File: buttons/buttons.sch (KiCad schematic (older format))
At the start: 9 parts, among them J1 header

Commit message: more library changes
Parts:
- J1: footprint HDRV9W63P0X254_1X9_2286X369X950P -> buttons:header
- S1, S2: footprint OS103011MS8QP1 -> buttons:switch
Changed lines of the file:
@@
 F 0 "S1" H 6928 2096 50  0000 L CNN
 F 1 "switch" H 6928 2005 50  0000 L CNN
-F 2 "OS103011MS8QP1" H 6950 2400 50  0001 L CNN
+F 2 "buttons:switch" H 6950 2400 50  0001 L CNN
 F 3 "https://www.ckswitches.com/media/1428/os.pdf" H 6950 2300 50  0001 L CNN
 F 4 "C & K COMPONENTS - OS103011MS8QP1 - SWITCH, SP3T, 0.1A, 12VDC, PCB, ON-ON-ON" H 6950 2200 50  0001 L CNN "Description"
@@
 F 0 "S2" H 6928 2946 50  0000 L CNN
 F 1 "switch" H 6928 2855 50  0000 L CNN
-F 2 "OS103011MS8QP1" H 6950 3250 50  0001 L CNN
+F 2 "buttons:switch" H 6950 3250 50  0001 L CNN
 F 3 "https://www.ckswitches.com/media/1428/os.pdf" H 6950 3150 50  0001 L CNN
 F 4 "C & K COMPONENTS - OS103011MS8QP1 - SWITCH, SP3T, 0.1A, 12VDC, PCB, ON-ON-ON" H 6950 3050 50  0001 L CNN "Description"
@@
 F 0 "J1" H 4842 2235 50  0000 C CNN
 F 1 "header" H 4842 2326 50  0000 C CNN
-F 2 "HDRV9W63P0X254_1X9_2286X369X950P" H 5200 3400 50  0001 L CNN
+F 2 "buttons:header" H 5200 3400 50  0001 L CNN
 F 3 "https://componentsearchengine.com/Datasheets/1/825433-9.pdf" H 5200 3300 50  0001 L CNN
 F 4 "MOD 2 PINHDR 1X9 P." H 5200 3200 50  0001 L CNN "Description"

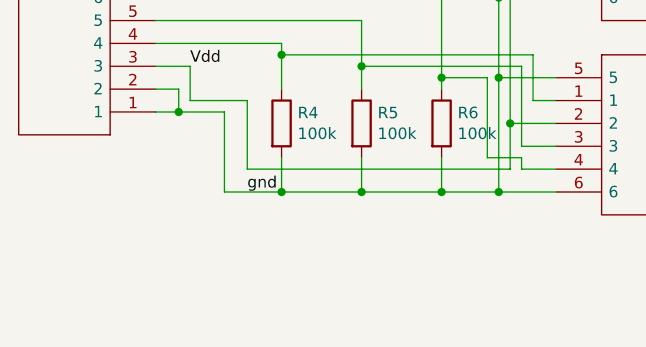
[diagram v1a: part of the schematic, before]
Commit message: cleaned up directories, silkscreen
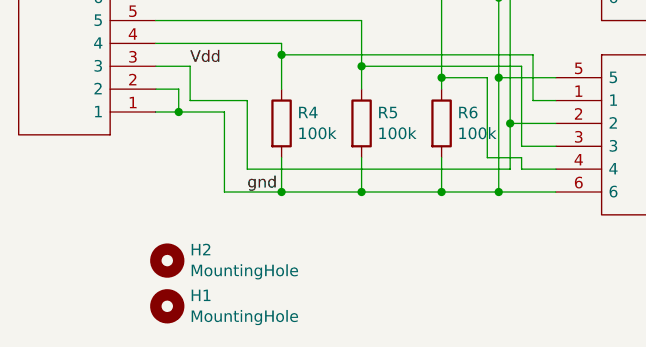
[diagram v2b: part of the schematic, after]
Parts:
- added H1, H2: MountingHole, buttons:MountingHole_2.5mm_Pad, symbol Mechanical:MountingHole
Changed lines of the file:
@@
+	1    0    0    -1
+$EndComp
+$Comp
+L Mechanical:MountingHole H2
+U 1 1 61672EB2
+P 4600 3950
+F 0 "H2" H 4700 3996 50  0000 L CNN
+F 1 "MountingHole" H 4700 3905 50  0000 L CNN
+F 2 "buttons:MountingHole_2.5mm_Pad" H 4600 3950 50  0001 C CNN
+F 3 "~" H 4600 3950 50  0001 C CNN
+	1    4600 3950
+	1    0    0    -1
+$EndComp
+$Comp
+L Mechanical:MountingHole H1
+U 1 1 616738A9
+P 4600 4150
+F 0 "H1" H 4700 4196 50  0000 L CNN
+F 1 "MountingHole" H 4700 4105 50  0000 L CNN
+F 2 "buttons:MountingHole_2.5mm_Pad" H 4600 4150 50  0001 C CNN
+F 3 "~" H 4600 4150 50  0001 C CNN
+	1    4600 4150
 	1    0    0    -1
 $EndComp

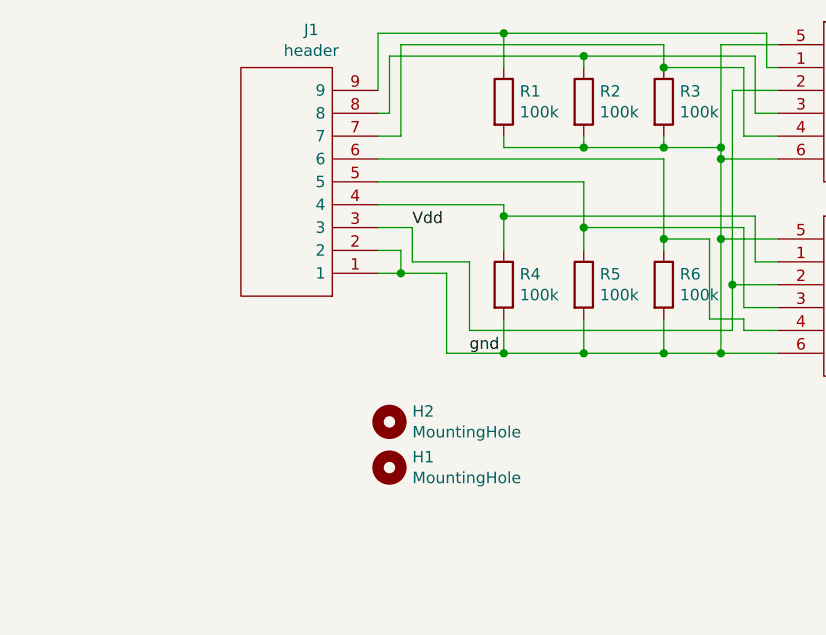
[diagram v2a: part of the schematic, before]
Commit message: Added reset button, fixed 7seg pin order
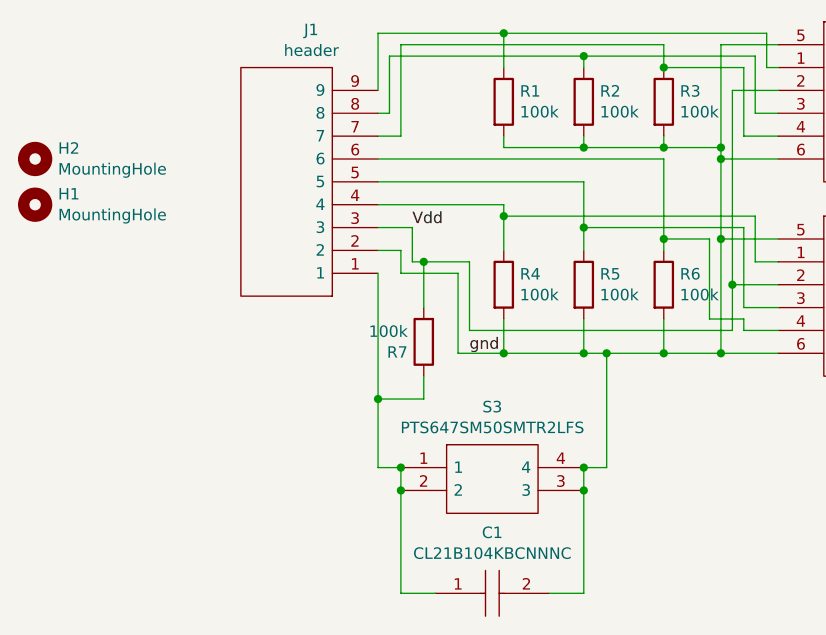
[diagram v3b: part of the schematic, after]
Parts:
- added C1: CL21B104KBCNNNC, CAPC2012X95N, symbol SamacSys_Parts:CL21B104KBCNNNC
- added R7: 100k, SamacSys_Parts:RESC3116X70N, symbol Device:R
- added S3: PTS647SM50SMTR2LFS, PTS647SM50SMTR2LFS, symbol SamacSys_Parts:PTS647SM50SMTR2LFS
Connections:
- net Vdd: now also R7.2
- net gnd: now also C1.2, S3.3, S3.4; no longer J1.1
- new net: C1.1, J1.1, R7.1, S3.1, S3.2
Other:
- moved on the sheet: H1, H2
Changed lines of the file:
@@
 $EndComp
-Wire Wire Line
-	4550 3300 4650 3300
 Wire Wire Line
 	6050 3650 6050 3150
@@
 Wire Wire Line
 	4700 3100 4700 3250
-Wire Wire Line
-	4650 3300 4850 3300
-Wire Wire Line
-	4850 3300 4850 3650
-Wire Wire Line
-	4850 3650 5100 3650
-Connection ~ 4650 3300
 Connection ~ 6050 3650
 Wire Wire Line
-	4700 3250 4950 3250
+	4700 3250 4750 3250
 Wire Wire Line
 	4950 3250 4950 3550
@@
 Connection ~ 5450 3650
 Wire Wire Line
-	5450 3650 5800 3650
+	5450 3650 5550 3650
 Wire Wire Line
 	5800 3500 5800 3650
@@
 Wire Wire Line
 	5100 3500 5100 3650
-Connection ~ 5100 3650
 Wire Wire Line
 	5100 3650 5450 3650
@@
 L Mechanical:MountingHole H2
 U 1 1 61672EB2
-P 4600 3950
-F 0 "H2" H 4700 3996 50  0000 L CNN
-F 1 "MountingHole" H 4700 3905 50  0000 L CNN
-F 2 "buttons:MountingHole_2.5mm_Pad" H 4600 3950 50  0001 C CNN
-F 3 "~" H 4600 3950 50  0001 C CNN
-	1    4600 3950
+P 3050 2800
+F 0 "H2" H 3150 2846 50  0000 L CNN
+F 1 "MountingHole" H 3150 2755 50  0000 L CNN
+F 2 "buttons:MountingHole_2.5mm_Pad" H 3050 2800 50  0001 C CNN
+F 3 "~" H 3050 2800 50  0001 C CNN
+	1    3050 2800
 	1    0    0    -1
 $EndComp
@@
 L Mechanical:MountingHole H1
 U 1 1 616738A9
-P 4600 4150
-F 0 "H1" H 4700 4196 50  0000 L CNN
-F 1 "MountingHole" H 4700 4105 50  0000 L CNN
-F 2 "buttons:MountingHole_2.5mm_Pad" H 4600 4150 50  0001 C CNN
-F 3 "~" H 4600 4150 50  0001 C CNN
-	1    4600 4150
-	1    0    0    -1
-$EndComp
+P 3050 3000
+F 0 "H1" H 3150 3046 50  0000 L CNN
+F 1 "MountingHole" H 3150 2955 50  0000 L CNN
+F 2 "buttons:MountingHole_2.5mm_Pad" H 3050 3000 50  0001 C CNN
+F 3 "~" H 3050 3000 50  0001 C CNN
+	1    3050 3000
+	1    0    0    -1
+$EndComp
+Wire Wire Line
+	4550 4150 4650 4150
+Wire Wire Line
+	4650 4250 4650 4150
+$Comp
+L Device:R R7
+U 1 1 616971F3
+P 4750 3600
+F 0 "R7" H 4820 3646 50  0000 L CNN
+F 1 "100k" H 4820 3555 50  0000 L CNN
+F 2 "SamacSys_Parts:RESC3116X70N" V 4680 3600 50  0001 C CNN
+F 3 "~" H 4750 3600 50  0001 C CNN
+	1    4750 3600
+	-1   0    0    1
+$EndComp
+Wire Wire Line
+	4550 3300 4550 3850
+Wire Wire Line
+	4900 3650 5100 3650
+Connection ~ 5100 3650
+Wire Wire Line
+	4900 3650 4900 3300
+Wire Wire Line
+	4650 3300 4900 3300
+Wire Wire Line
+	4750 3450 4750 3250
+Connection ~ 4750 3250
+Wire Wire Line
+	4750 3250 4950 3250
+Wire Wire Line
+	4750 3750 4750 3850
+Wire Wire Line
+	4750 3850 4550 3850
+Connection ~ 4550 3850
+Wire Wire Line
+	4550 3850 4550 4150
+Wire Wire Line
+	5550 3650 5550 4150
+Wire Wire Line
+	5550 4150 5450 4150
+Connection ~ 5550 3650
+Wire Wire Line
+	5550 3650 5800 3650
+Wire Wire Line
+	5450 4250 5450 4150
+$Comp
+L SamacSys_Parts:CL21B104KBCNNNC C1
+U 1 1 616A684B
+P 4800 4700
+F 0 "C1" H 5050 4965 50  0000 C CNN
+F 1 "CL21B104KBCNNNC" H 5050 4874 50  0000 C CNN
+F 2 "CAPC2012X95N" H 5150 4750 50  0001 L CNN
+F 3 "http://www.samsungsem.com/kr/support/product-search/mlcc/CL21B104KBCNNNC.jsp" H 5150 4650 50  0001 L CNN
+F 4 "Samsung Electro-Mechanics 0805 (2012M) 100nF Multilayer Ceramic Capacitor MLCC 50V dc +/-10% SMD CL21B104KBCNNNC" H 5150 4550 50  0001 L CNN "Description"
+F 5 "0.95" H 5150 4450 50  0001 L CNN "Height"
+F 6 "187-CL21B104KBCNNNC" H 5150 4350 50  0001 L CNN "Mouser Part Number"
+F 7 "https://www.mouser.co.uk/ProductDetail/Samsung-Electro-Mechanics/CL21B104KBCNNNC?qs=349EhDEZ59pEfpnm5yBEmQ%3D%3D" H 5150 4250 50  0001 L CNN "Mouser Price/Stock"
+F 8 "Samsung Electro-Mechanics" H 5150 4150 50  0001 L CNN "Manufacturer_Name"
+F 9 "CL21B104KBCNNNC" H 5150 4050 50  0001 L CNN "Manufacturer_Part_Number"
+	1    4800 4700
+	1    0    0    -1
+$EndComp
+$Comp
+L SamacSys_Parts:PTS647SM50SMTR2LFS S3
+U 1 1 616AAC5F
+P 4650 4150
+F 0 "S3" H 5050 4415 50  0000 C CNN
+F 1 "PTS647SM50SMTR2LFS" H 5050 4324 50  0000 C CNN
+F 2 "PTS647SM50SMTR2LFS" H 5300 4250 50  0001 L CNN
+F 3 "https://www.ckswitches.com/media/2567/pts647.pdf" H 5300 4150 50  0001 L CNN
+F 4 "Tactile Switches 50mA 12VDC, 1.8N 5.0mm H, G leads" H 5300 4050 50  0001 L CNN "Description"
+F 5 "5.25" H 5300 3950 50  0001 L CNN "Height"
+F 6 "611-PTS647SM50SMTR2L" H 5300 3850 50  0001 L CNN "Mouser Part Number"
+F 7 "https://www.mouser.co.uk/ProductDetail/CK/PTS647SM50SMTR2LFS?qs=PqoDHHvF64%252BjK4ZB7f42kw%3D%3D" H 5300 3750 50  0001 L CNN "Mouser Price/Stock"
+F 8 "C & K COMPONENTS" H 5300 3650 50  0001 L CNN "Manufacturer_Name"
+F 9 "PTS647SM50SMTR2LFS" H 5300 3550 50  0001 L CNN "Manufacturer_Part_Number"
+	1    4650 4150
+	1    0    0    -1
+$EndComp
+Connection ~ 4650 4150
+Connection ~ 5450 4150
+Wire Wire Line
+	5300 4700 5450 4700
+Wire Wire Line
+	5450 4700 5450 4250
+Connection ~ 5450 4250
+Wire Wire Line
+	4800 4700 4650 4700
+Wire Wire Line
+	4650 4700 4650 4250
+Connection ~ 4650 4250
 $EndSCHEMATC

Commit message: final Rev1 changes. increased heatsink area, flipped LEDs again, increased button mount hole size
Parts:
- C1: symbol SamacSys_Parts:CL21B104KBCNNNC -> buttons-rescue:CL21B104KBCNNNC-SamacSys_Parts
- H1, H2: footprint buttons:MountingHole_2.5mm_Pad -> buttons:MountingHole_3.2mm_M3_Pad
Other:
- moved on the sheet: H1
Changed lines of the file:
@@
-$EndComp
-$Comp
-L Mechanical:MountingHole H2
-U 1 1 61672EB2
-P 3050 2800
-F 0 "H2" H 3150 2846 50  0000 L CNN
-F 1 "MountingHole" H 3150 2755 50  0000 L CNN
-F 2 "buttons:MountingHole_2.5mm_Pad" H 3050 2800 50  0001 C CNN
-F 3 "~" H 3050 2800 50  0001 C CNN
-	1    3050 2800
-	1    0    0    -1
 $EndComp
 $Comp
 L Mechanical:MountingHole H1
 U 1 1 616738A9
-P 3050 3000
-F 0 "H1" H 3150 3046 50  0000 L CNN
-F 1 "MountingHole" H 3150 2955 50  0000 L CNN
-F 2 "buttons:MountingHole_2.5mm_Pad" H 3050 3000 50  0001 C CNN
-F 3 "~" H 3050 3000 50  0001 C CNN
-	1    3050 3000
+P 3050 3200
+F 0 "H1" H 3150 3246 50  0000 L CNN
+F 1 "MountingHole" H 3150 3155 50  0000 L CNN
+F 2 "buttons:MountingHole_3.2mm_M3_Pad" H 3050 3200 50  0001 C CNN
+F 3 "~" H 3050 3200 50  0001 C CNN
+	1    3050 3200
 	1    0    0    -1
 $EndComp
@@
 	5450 4250 5450 4150
 $Comp
-L SamacSys_Parts:CL21B104KBCNNNC C1
+L buttons-rescue:CL21B104KBCNNNC-SamacSys_Parts C1
 U 1 1 616A684B
 P 4800 4700
@@
 	4650 4700 4650 4250
 Connection ~ 4650 4250
+$Comp
+L Mechanical:MountingHole H2
+U 1 1 6169FA5D
+P 3050 3000
+F 0 "H2" H 3150 3046 50  0000 L CNN
+F 1 "MountingHole" H 3150 2955 50  0000 L CNN
+F 2 "buttons:MountingHole_3.2mm_M3_Pad" H 3050 3000 50  0001 C CNN
+F 3 "~" H 3050 3000 50  0001 C CNN
+	1    3050 3000
+	1    0    0    -1
+$EndComp
 $EndSCHEMATC

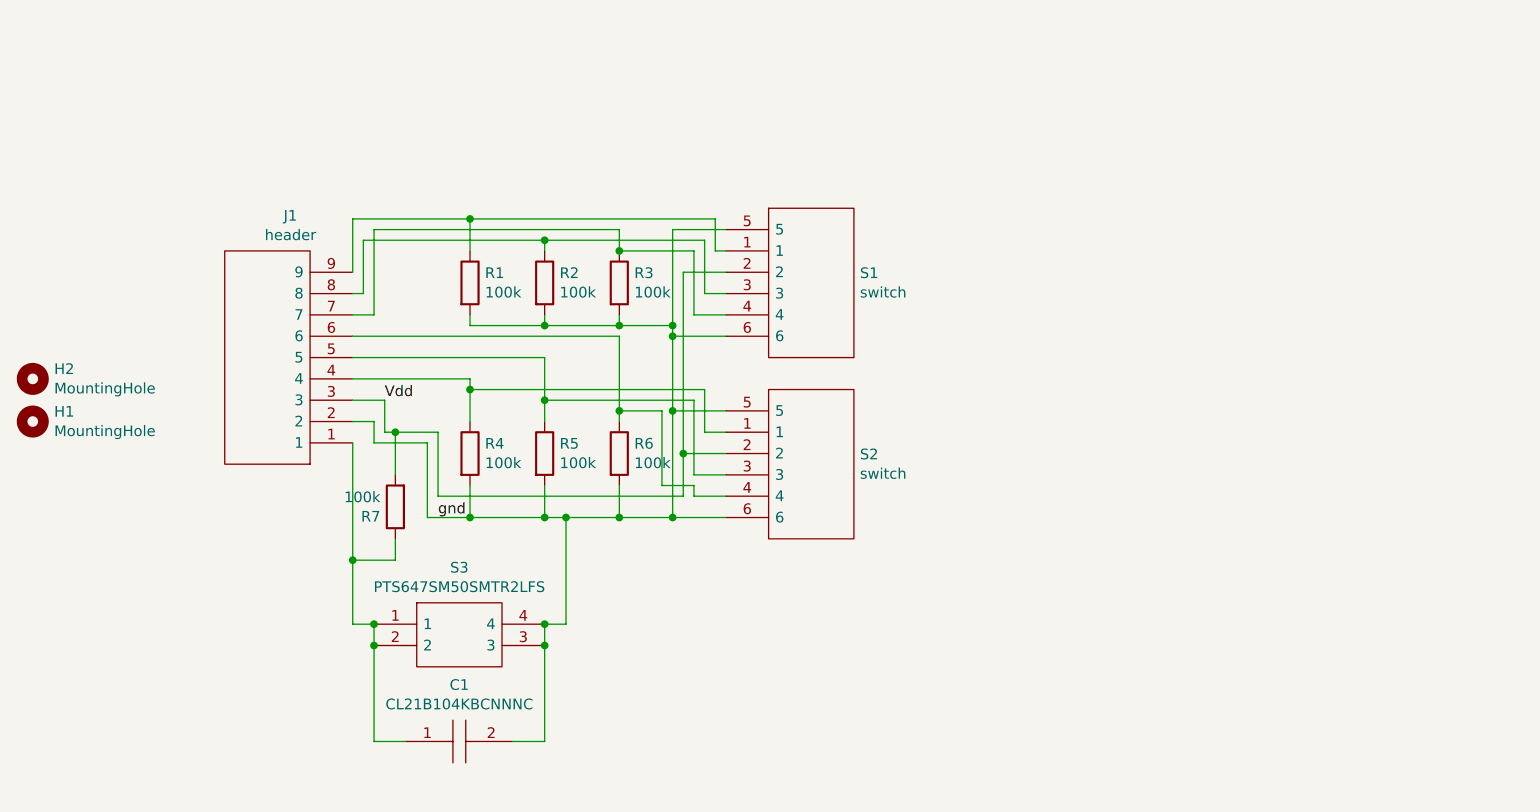
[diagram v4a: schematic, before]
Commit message: added two more buttons
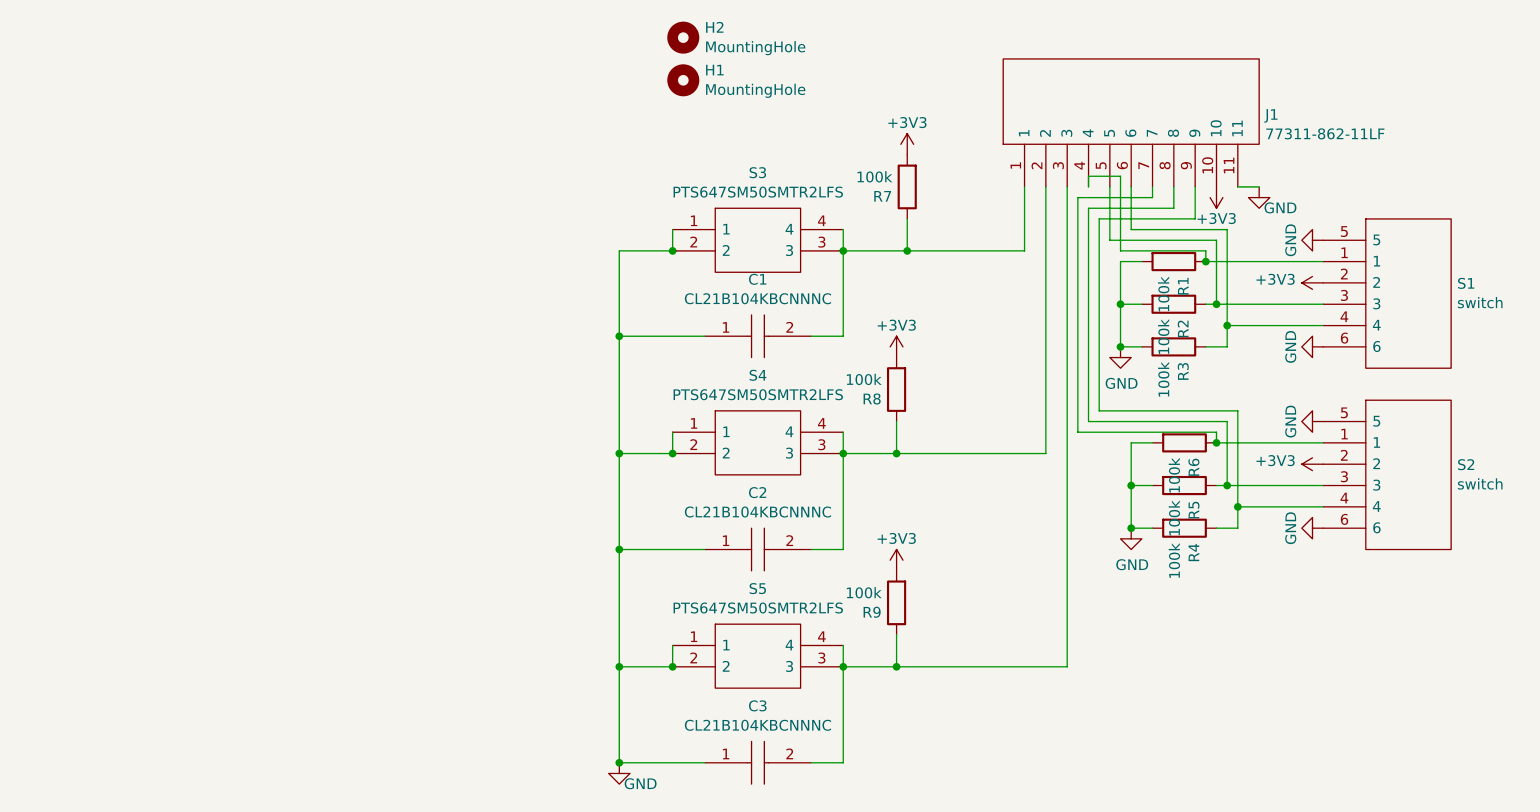
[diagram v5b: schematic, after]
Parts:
- removed J1: header, buttons:header, symbol 477parts:header
- added C2, C3: CL21B104KBCNNNC, CAPC2012X95N, symbol buttons-rescue:CL21B104KBCNNNC-SamacSys_Parts
- added J1: 77311-862-11LF, buttons:HDRV11W62P0X254_1X11_2794X240X853P, symbol 477parts:77311-862-11LF
- added R8, R9: 100k, SamacSys_Parts:RESC3116X70N, symbol Device:R
- added S4, S5: PTS647SM50SMTR2LFS, PTS647SM50SMTR2LFS, symbol SamacSys_Parts:PTS647SM50SMTR2LFS
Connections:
- net at R1.1, S1.1: now also J1.4
- net at R2.1, S1.3: now also J1.5
- net at R3.1, S1.4: now also J1.6
- net at S2.1: now also R6.1, J1.7; no longer R4.1
- net at R5.1, S2.3: now also J1.8
- net at S2.4: now also R4.1, J1.9; no longer R6.1
- net GND: now reaches C1.1, S3.1, S3.2
- net GND: now also R1.2, R2.2, R3.2, R4.2, R5.2, R6.2, S1.5, S1.6, S2.5, S2.6, C2.1, C3.1, J1.11, S4.1, S4.2, S5.1, S5.2; no longer R7.1
- net Vdd renamed +3V3
- net +3V3: now also J1.10, R8.2, R9.2
- removed net gnd: C1.2, R1.2, R2.2, R3.2, R4.2, R5.2, R6.2, S1.5, S1.6, S2.5, S2.6, S3.3, S3.4
- new net: C1.2, J1.1, R7.1, S3.3, S3.4
- new net: C2.2, J1.2, R8.1, S4.3, S4.4
- new net: C3.2, J1.3, R9.1, S5.3, S5.4
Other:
- moved on the sheet: C1, H1, H2, R1, R2, R3, R4, R5, R6, R7, S1, S2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
